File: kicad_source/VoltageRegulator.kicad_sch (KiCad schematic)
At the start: 25 parts, among them U12 IFX91041EFJ

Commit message: updated layout
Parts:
- C36, C42, C43: footprint capacitors:TantalC_SizeD_EIA-7343_Wave -> Capacitor_Tantalum_SMD:CP_EIA-7343-15_Kemet-W
- C37, C38, C39, C40, C41, C44: footprint capacitors:C_0603 -> Capacitor_SMD:C_0603_1608Metric
- D6: footprint diodes:SMA_Standard -> Diode_SMD:D_SMA
- MECH10, MECH11, MECH12, MECH13, MECH14, MECH5, MECH6, MECH7, MECH8, MECH9: footprint MECH_mounting_holes:MHP_3.2_5.0 -> generationmake:MHP_3.2_5.8
- R42, R43, R44: footprint resistors:R_0603 -> Resistor_SMD:R_0603_1608Metric
- U12: footprint SOIC:SOIC-8-1EP_3.9x4.9mm_Pitch1.27mm -> Package_SO:SOIC-8-1EP_3.9x4.9mm_P1.27mm_EP2.29x3mm
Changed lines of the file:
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@@
     (property "Reference" "U12" (id 0) (at 130.81 76.454 0))
     (property "Value" "IFX91041EFJ" (id 1) (at 130.81 78.7654 0))
-    (property "Footprint" "SOIC:SOIC-8-1EP_3.9x4.9mm_Pitch1.27mm" (id 2) (at 128.27 100.33 0)
+    (property "Footprint" "Package_SO:SOIC-8-1EP_3.9x4.9mm_P1.27mm_EP2.29x3mm" (id 2) (at 128.27 100.33 0)
       (effects (font (size 1.27 1.27)) hide)
     )
@@
       (effects (font (size 1.27 1.27)) (justify left))
     )
-    (property "Footprint" "capacitors:C_0603" (id 2) (at 93.98 105.41 0)
+    (property "Footprint" "Capacitor_SMD:C_0603_1608Metric" (id 2) (at 93.98 105.41 0)
       (effects (font (size 1.27 1.27)) hide)
     )
@@
       (effects (font (size 1.27 1.27)) (justify left))
     )
-    (property "Footprint" "resistors:R_0603" (id 2) (at 93.98 114.3 0)
+    (property "Footprint" "Resistor_SMD:R_0603_1608Metric" (id 2) (at 93.98 114.3 0)
       (effects (font (size 1.27 1.27)) hide)
     )
@@
       (effects (font (size 1.27 1.27)) (justify left))
     )
-    (property "Footprint" "capacitors:C_0603" (id 2) (at 82.55 110.49 0)
+    (property "Footprint" "Capacitor_SMD:C_0603_1608Metric" (id 2) (at 82.55 110.49 0)
       (effects (font (size 1.27 1.27)) hide)
     )
@@
       (effects (font (size 1.27 1.27)) (justify left))
     )
-    (property "Footprint" "capacitors:C_0603" (id 2) (at 96.52 86.36 0)
+    (property "Footprint" "Capacitor_SMD:C_0603_1608Metric" (id 2) (at 96.52 86.36 0)
       (effects (font (size 1.27 1.27)) hide)
     )
@@
       (effects (font (size 1.27 1.27)) (justify left))
     )
-    (property "Footprint" "capacitors:C_0603" (id 2) (at 151.13 115.57 0)
+    (property "Footprint" "Capacitor_SMD:C_0603_1608Metric" (id 2) (at 151.13 115.57 0)
       (effects (font (size 1.27 1.27)) hide)
     )
@@
       (effects (font (size 1.27 1.27)) (justify left))
     )
-    (property "Footprint" "resistors:R_0603" (id 2) (at 181.61 115.57 0)
+    (property "Footprint" "Resistor_SMD:R_0603_1608Metric" (id 2) (at 181.61 115.57 0)
       (effects (font (size 1.27 1.27)) hide)
     )
@@
       (effects (font (size 1.27 1.27)) (justify left))
     )
-    (property "Footprint" "resistors:R_0603" (id 2) (at 181.61 106.68 0)
+    (property "Footprint" "Resistor_SMD:R_0603_1608Metric" (id 2) (at 181.61 106.68 0)
       (effects (font (size 1.27 1.27)) hide)
     )
@@
       (effects (font (size 1.27 1.27)) (justify left))
     )
-    (property "Footprint" "capacitors:C_0603" (id 2) (at 152.4 93.98 0)
+    (property "Footprint" "Capacitor_SMD:C_0603_1608Metric" (id 2) (at 152.4 93.98 0)
       (effects (font (size 1.27 1.27)) hide)
     )
@@
       (effects (font (size 1.27 1.27)) (justify left))
     )
-    (property "Footprint" "capacitors:TantalC_SizeD_EIA-7343_Wave" (id 2) (at 200.66 105.41 0)
+    (property "Footprint" "Capacitor_Tantalum_SMD:CP_EIA-7343-15_Kemet-W" (id 2) (at 200.66 105.41 0)
       (effects (font (size 1.27 1.27)) hide)
     )
@@
       (effects (font (size 1.27 1.27)) (justify left))
     )
-    (property "Footprint" "capacitors:TantalC_SizeD_EIA-7343_Wave" (id 2) (at 215.9 105.41 0)
+    (property "Footprint" "Capacitor_Tantalum_SMD:CP_EIA-7343-15_Kemet-W" (id 2) (at 215.9 105.41 0)
       (effects (font (size 1.27 1.27)) hide)
     )
@@
       (effects (font (size 1.27 1.27)) (justify left))
     )
-    (property "Footprint" "capacitors:TantalC_SizeD_EIA-7343_Wave" (id 2) (at 83.82 87.63 0)
+    (property "Footprint" "Capacitor_Tantalum_SMD:CP_EIA-7343-15_Kemet-W" (id 2) (at 83.82 87.63 0)
       (effects (font (size 1.27 1.27)) hide)
     )
@@
       (effects (font (size 1.27 1.27)) (justify left))
     )
-    (property "Footprint" "capacitors:C_0603" (id 2) (at 228.6 104.14 0)
+    (property "Footprint" "Capacitor_SMD:C_0603_1608Metric" (id 2) (at 228.6 104.14 0)
       (effects (font (size 1.27 1.27)) hide)
     )
@@
       (effects (font (size 1.27 1.27)) (justify left))
     )
-    (property "Footprint" "diodes:SMA_Standard" (id 2) (at 154.94 99.06 90)
+    (property "Footprint" "Diode_SMD:D_SMA" (id 2) (at 154.94 99.06 90)
       (effects (font (size 1.27 1.27)) hide)
     )
@@
       (effects (font (size 1.27 1.27)) (justify left))
     )
-    (property "Footprint" "MECH_mounting_holes:MHP_3.2_5.0" (id 2) (at 30.48 138.43 0)
+    (property "Footprint" "generationmake:MHP_3.2_5.8" (id 2) (at 30.48 138.43 0)
       (effects (font (size 1.27 1.27)) hide)
     )
@@
       (effects (font (size 1.27 1.27)) (justify left))
     )
-    (property "Footprint" "MECH_mounting_holes:MHP_3.2_5.0" (id 2) (at 30.48 144.78 0)
+    (property "Footprint" "generationmake:MHP_3.2_5.8" (id 2) (at 30.48 144.78 0)
       (effects (font (size 1.27 1.27)) hide)
     )
@@
       (effects (font (size 1.27 1.27)) (justify left))
     )
-    (property "Footprint" "MECH_mounting_holes:MHP_3.2_5.0" (id 2) (at 30.48 151.13 0)
+    (property "Footprint" "generationmake:MHP_3.2_5.8" (id 2) (at 30.48 151.13 0)
       (effects (font (size 1.27 1.27)) hide)
     )
@@
       (effects (font (size 1.27 1.27)) (justify left))
     )
-    (property "Footprint" "MECH_mounting_holes:MHP_3.2_5.0" (id 2) (at 30.48 157.48 0)
+    (property "Footprint" "generationmake:MHP_3.2_5.8" (id 2) (at 30.48 157.48 0)
       (effects (font (size 1.27 1.27)) hide)
     )
@@
       (effects (font (size 1.27 1.27)) (justify left))
     )
-    (property "Footprint" "MECH_mounting_holes:MHP_3.2_5.0" (id 2) (at 66.04 138.43 0)
+    (property "Footprint" "generationmake:MHP_3.2_5.8" (id 2) (at 66.04 138.43 0)
       (effects (font (size 1.27 1.27)) hide)
     )
@@
       (effects (font (size 1.27 1.27)) (justify left))
     )
-    (property "Footprint" "MECH_mounting_holes:MHP_3.2_5.0" (id 2) (at 66.04 144.78 0)
+    (property "Footprint" "generationmake:MHP_3.2_5.8" (id 2) (at 66.04 144.78 0)
       (effects (font (size 1.27 1.27)) hide)
     )
@@
       (effects (font (size 1.27 1.27)) (justify left))
     )
-    (property "Footprint" "MECH_mounting_holes:MHP_3.2_5.0" (id 2) (at 66.04 151.13 0)
+    (property "Footprint" "generationmake:MHP_3.2_5.8" (id 2) (at 66.04 151.13 0)
       (effects (font (size 1.27 1.27)) hide)
     )
@@
       (effects (font (size 1.27 1.27)) (justify left))
     )
-    (property "Footprint" "MECH_mounting_holes:MHP_3.2_5.0" (id 2) (at 66.04 157.48 0)
+    (property "Footprint" "generationmake:MHP_3.2_5.8" (id 2) (at 66.04 157.48 0)
       (effects (font (size 1.27 1.27)) hide)
     )
@@
       (effects (font (size 1.27 1.27)) (justify left))
     )
-    (property "Footprint" "MECH_mounting_holes:MHP_3.2_5.0" (id 2) (at 66.04 163.83 0)
+    (property "Footprint" "generationmake:MHP_3.2_5.8" (id 2) (at 66.04 163.83 0)
       (effects (font (size 1.27 1.27)) hide)
     )
@@
       (effects (font (size 1.27 1.27)) (justify left))
     )
-    (property "Footprint" "MECH_mounting_holes:MHP_3.2_5.0" (id 2) (at 66.04 170.18 0)
-      (effects (font (size 1.27 1.27)) hide)
-    )
+    (property "Footprint" "generationmake:MHP_3.2_5.8" (id 2) (at 66.04 170.18 0)
+      (effects (font (size 1.27 1.27)) hide)
+    )

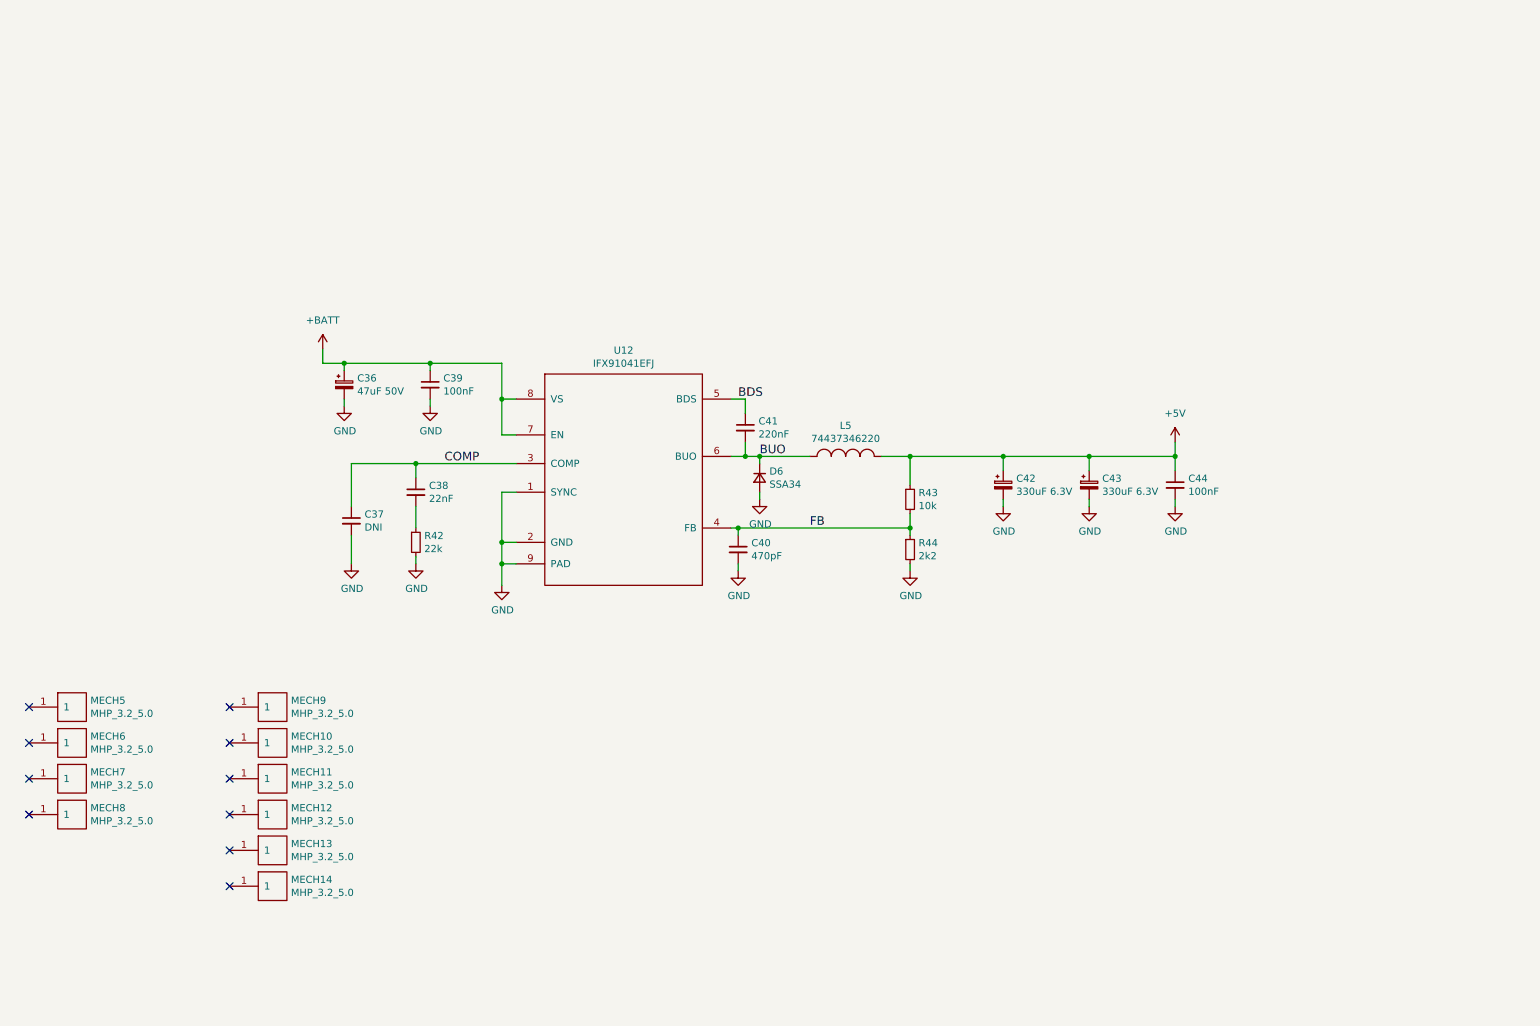
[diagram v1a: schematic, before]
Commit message: moved input circuit to voltage regulator side
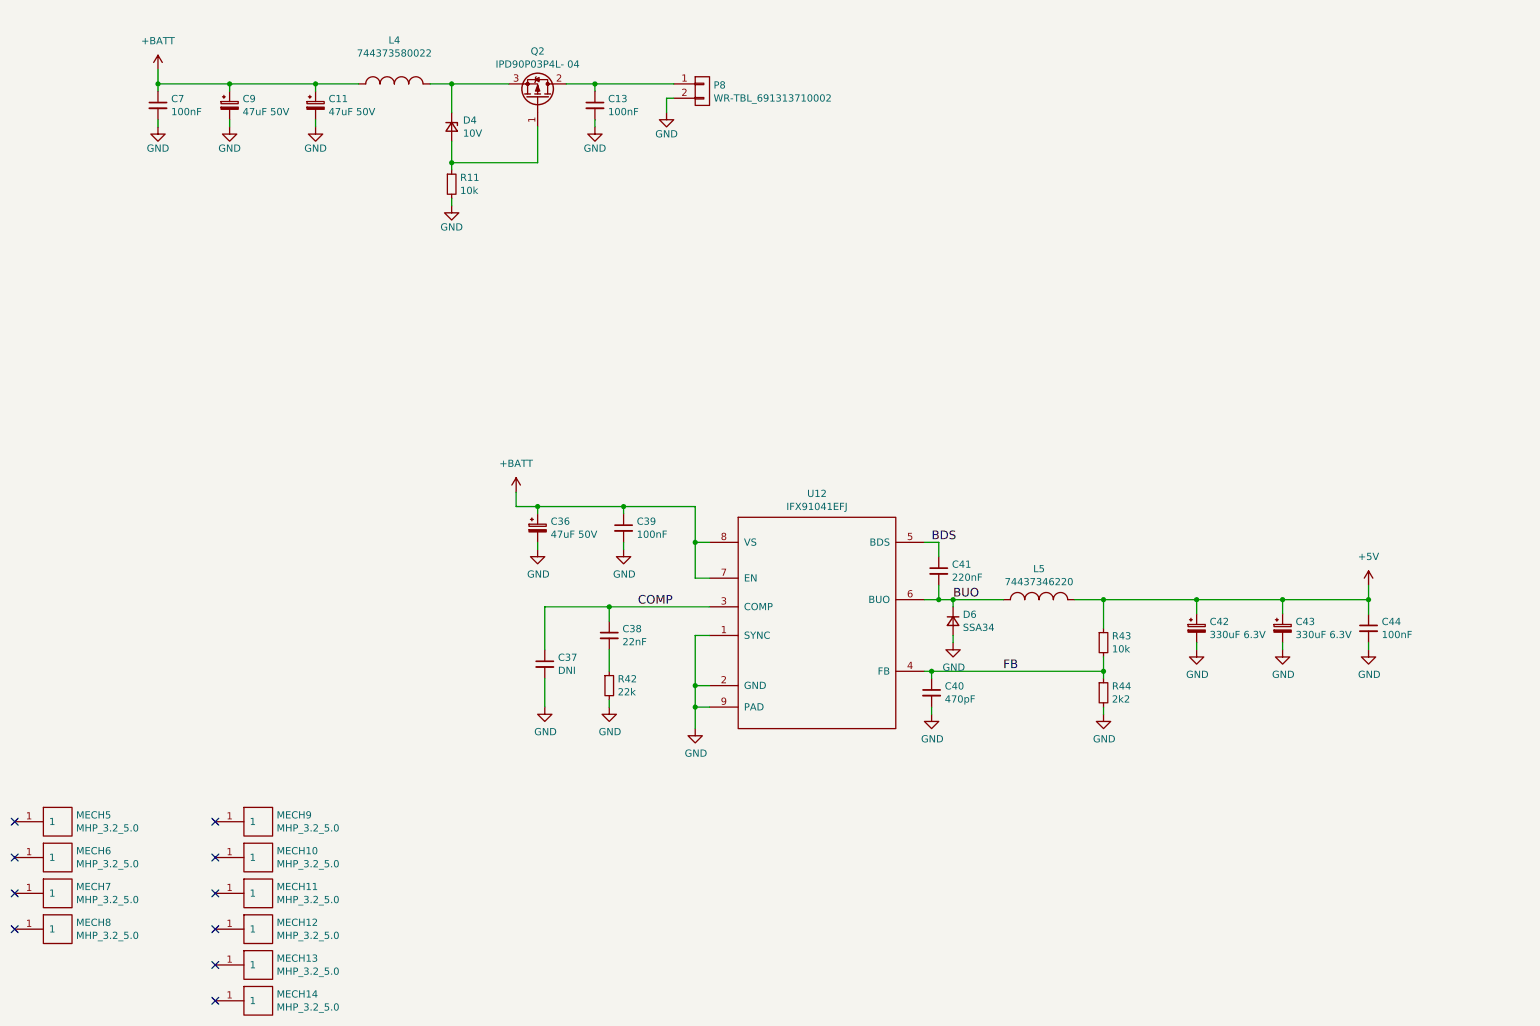
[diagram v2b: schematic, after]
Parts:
- added C11, C9: 47uF 50V, Capacitor_Tantalum_SMD:CP_EIA-7343-15_Kemet-W, symbol Device:C_Polarized_Small
- added C13, C7: 100nF, Capacitor_SMD:C_0603_1608Metric, symbol Device:C_Small
- added D4: 10V, Diode_SMD:D_SOD-123, symbol Device:D_Zener_Small
- added L4: 744373580022, L_power:WE-LHMI80xx, symbol OpenCyphalRobotController07-rescue:74437346082-L_power
- added P8: WR-TBL_691313710002, CON_wuerth:WR-TBL_691313710002, symbol OpenCyphalRobotController07-rescue:WR-TBL_691313710002-mechanical-connectors
- added Q2: IPD90P03P4L- 04, SOT_TO:TO-252-2Lead, symbol Device:Q_PMOS_GDS
- added R11: 10k, Resistor_SMD:R_0603_1608Metric, symbol Device:R_Small
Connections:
- net +BATT: now also C11.1, C7.1, C9.1, L4.1
- net GND: now also C11.2, C13.2, C7.2, C9.2, P8.2 (P2), R11.2
- new net: C13.1, P8.1 (P1), Q2.2 (D)
- new net: D4.1 (K), L4.2, Q2.3 (S)
- new net: D4.2 (A), Q2.1 (G), R11.1
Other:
- moved on the sheet: C36, C37, C38, C39, C40, C41, C42, C43, C44, D6, L5, MECH10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

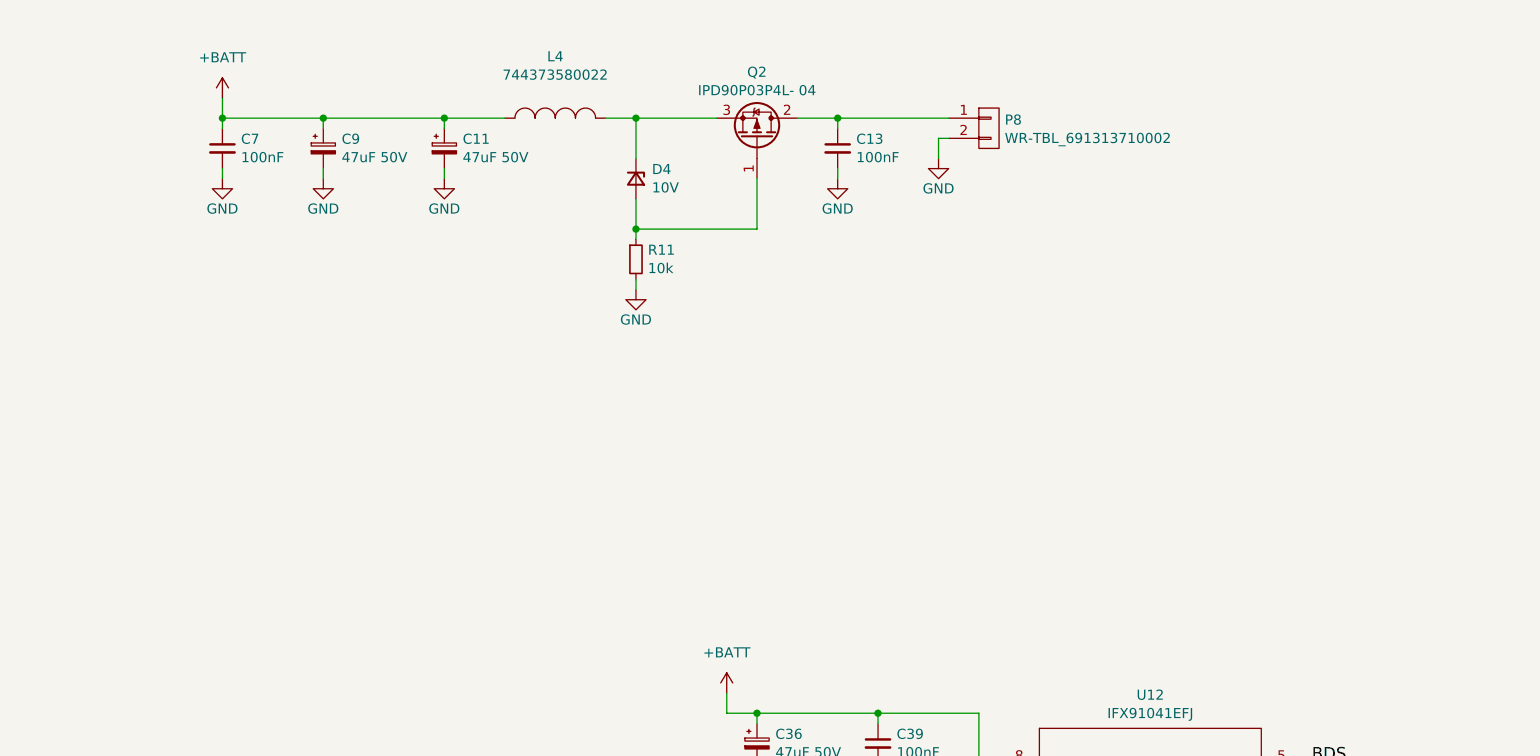
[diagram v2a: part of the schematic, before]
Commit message: added INA226
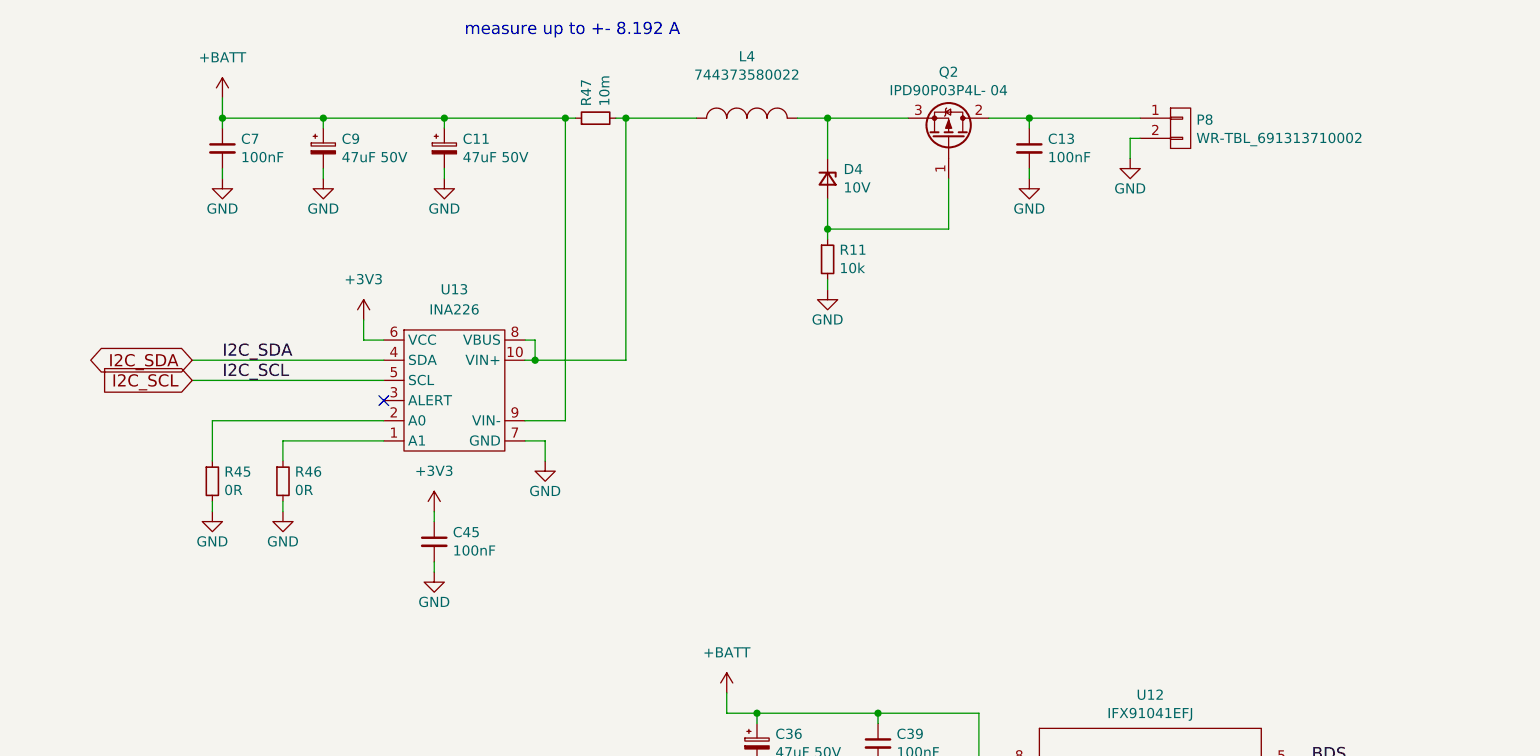
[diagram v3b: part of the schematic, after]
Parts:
- added C45: 100nF, Capacitor_SMD:C_0603_1608Metric, symbol Device:C_Small
- added R45, R46: 0R, Resistor_SMD:R_0603_1608Metric, symbol Device:R_Small
- added R47: 10m, Resistor_SMD:R_1206_3216Metric, symbol Device:R_Small
- added U13: INA226, Package_SO:MSOP-10_3x3mm_P0.5mm, symbol generationmake:INA226
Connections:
- net +BATT: now also R47.1, U13.9 (VIN-); no longer L4.1
- net GND: now also C45.2, R45.2, R46.2, U13.7 (GND)
- new net: R46.1, U13.1 (A1)
- new net: L4.1, R47.2, U13.10 (VIN+), U13.8 (VBUS)
- new net: R45.1, U13.2 (A0)
- new net +3V3: C45.1, U13.6 (VCC)
- new net I2C_SCL: U13.5 (SCL)
- new net I2C_SDA: U13.4 (SDA)
- no-connect marks 10 -> 11
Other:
- note added: "measure up to +- 8.192 A"
- moved on the sheet: C13, D4, L4, P8, Q2, R11

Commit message: added page with outputs
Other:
- title: OpenCyphalRobotController07 -> CyphalRobotController07/CAN
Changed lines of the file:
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@@
   (paper "A4")
   (title_block
-    (title "OpenCyphalRobotController07")
-    (date "2023-07-24")
+    (title "CyphalRobotController07/CAN")
+    (date "2023-10-01")
     (rev "0.1")
     (company "generationmake")
